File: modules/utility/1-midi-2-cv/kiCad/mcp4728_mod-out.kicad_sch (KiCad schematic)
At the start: 18 parts, among them U3 MCP4728, U4 TL074

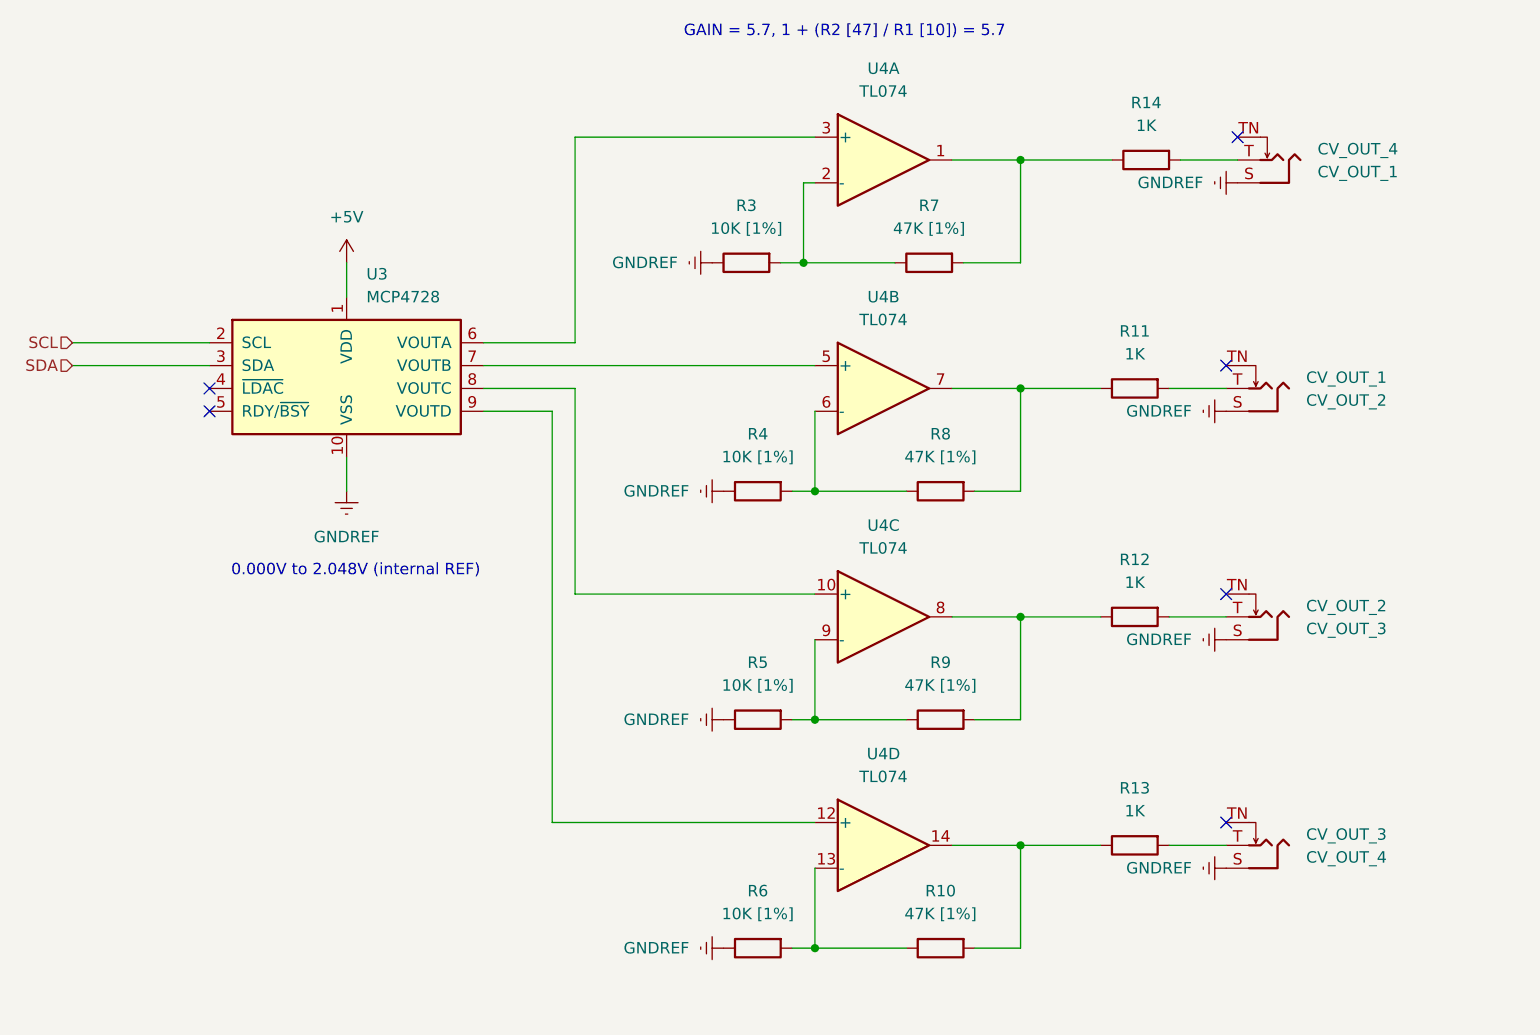
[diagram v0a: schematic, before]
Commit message: add panels, redo gerbers for distorted daisy
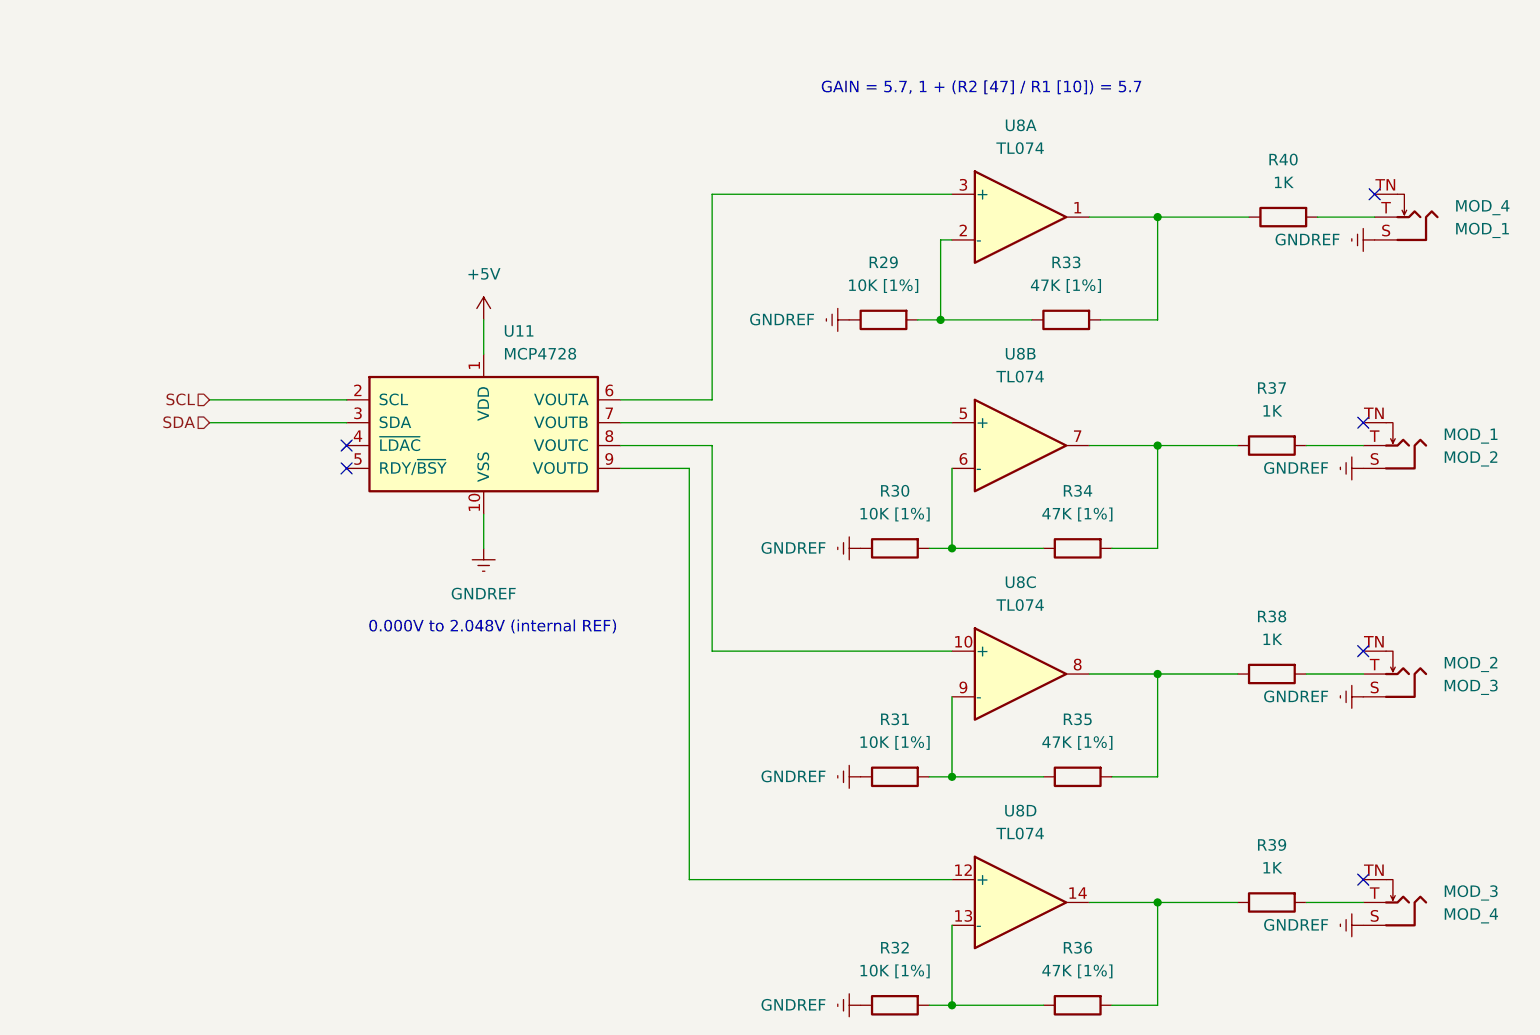
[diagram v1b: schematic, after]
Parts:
- removed CV_OUT_1: CV_OUT_2, Synth:Jack_3.5mm_QingPu_WQP-PJ398SM_Vertical_CircularHoles, symbol synth:AudioJack_Mono_3.5mm
- removed CV_OUT_2: CV_OUT_3, Synth:Jack_3.5mm_QingPu_WQP-PJ398SM_Vertical_CircularHoles, symbol synth:AudioJack_Mono_3.5mm
- removed CV_OUT_3: CV_OUT_4, Synth:Jack_3.5mm_QingPu_WQP-PJ398SM_Vertical_CircularHoles, symbol synth:AudioJack_Mono_3.5mm
- removed CV_OUT_4: CV_OUT_1, Synth:Jack_3.5mm_QingPu_WQP-PJ398SM_Vertical_CircularHoles, symbol synth:AudioJack_Mono_3.5mm
- removed R10, R7, R8, R9: 47K [1%], Synth:R_Default (DIN0207), symbol synth:R_Default
- removed R11, R12, R13, R14: 1K, Synth:R_Default (DIN0207), symbol synth:R_Default
- removed R3, R4, R5, R6: 10K [1%], Synth:R_Default (DIN0207), symbol synth:R_Default
- removed U3: MCP4728, Package_SO:MSOP-10_3x3mm_P0.5mm, symbol Analog_DAC:MCP4728
- removed U4: TL074, Package_SO:SOIC-14_3.9x8.7mm_P1.27mm, symbol Amplifier_Operational:TL074
- added MOD_1: MOD_2, Synth:Jack_3.5mm_QingPu_WQP-PJ398SM_Vertical_CircularHoles, symbol synth:AudioJack_Mono_3.5mm
- added MOD_2: MOD_3, Synth:Jack_3.5mm_QingPu_WQP-PJ398SM_Vertical_CircularHoles, symbol synth:AudioJack_Mono_3.5mm
- added MOD_3: MOD_4, Synth:Jack_3.5mm_QingPu_WQP-PJ398SM_Vertical_CircularHoles, symbol synth:AudioJack_Mono_3.5mm
- added MOD_4: MOD_1, Synth:Jack_3.5mm_QingPu_WQP-PJ398SM_Vertical_CircularHoles, symbol synth:AudioJack_Mono_3.5mm
- added R29, R30, R31, R32: 10K [1%], Synth:R_Default (DIN0207), symbol synth:R_Default
- added R33, R34, R35, R36: 47K [1%], Synth:R_Default (DIN0207), symbol synth:R_Default
- added R37, R38, R39, R40: 1K, Synth:R_Default (DIN0207), symbol synth:R_Default
- added U11: MCP4728, Package_SO:MSOP-10_3x3mm_P0.5mm, symbol Analog_DAC:MCP4728
- added U8: TL074, Package_SO:SOIC-14_3.9x8.7mm_P1.27mm, symbol Amplifier_Operational:TL074
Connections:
- net +5V: now also U11.1 (VDD)
- net GNDREF: now also MOD_1.S, MOD_2.S, MOD_3.S, MOD_4.S, R29.2, R30.2, R31.2, R32.2, U11.10 (VSS)
- net SCL: now also U11.2 (SCL)
- net SDA: now also U11.3 (SDA)
- new net: R32.1, R36.2, U8.13 (-)
- new net: U11.9 (VOUTD), U8.12 (+)
- new net: R36.1, R39.2, U8.14
- new net: R33.1, R40.2, U8.1
- new net: R29.1, R33.2, U8.2 (-)
- new net: U11.6 (VOUTA), U8.3 (+)
- new net: R34.1, R37.2, U8.7
- new net: R30.1, R34.2, U8.6 (-)
- new net: MOD_4.T, R40.1
- new net: MOD_1.T, R37.1
- new net: MOD_2.T, R38.1
- new net: R35.1, R38.2, U8.8
- new net: MOD_3.T, R39.1
- new net: U11.8 (VOUTC), U8.10 (+)
- new net: R31.1, R35.2, U8.9 (-)
- new net: U11.7 (VOUTB), U8.5 (+)
